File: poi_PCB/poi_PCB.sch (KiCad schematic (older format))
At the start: 43 parts

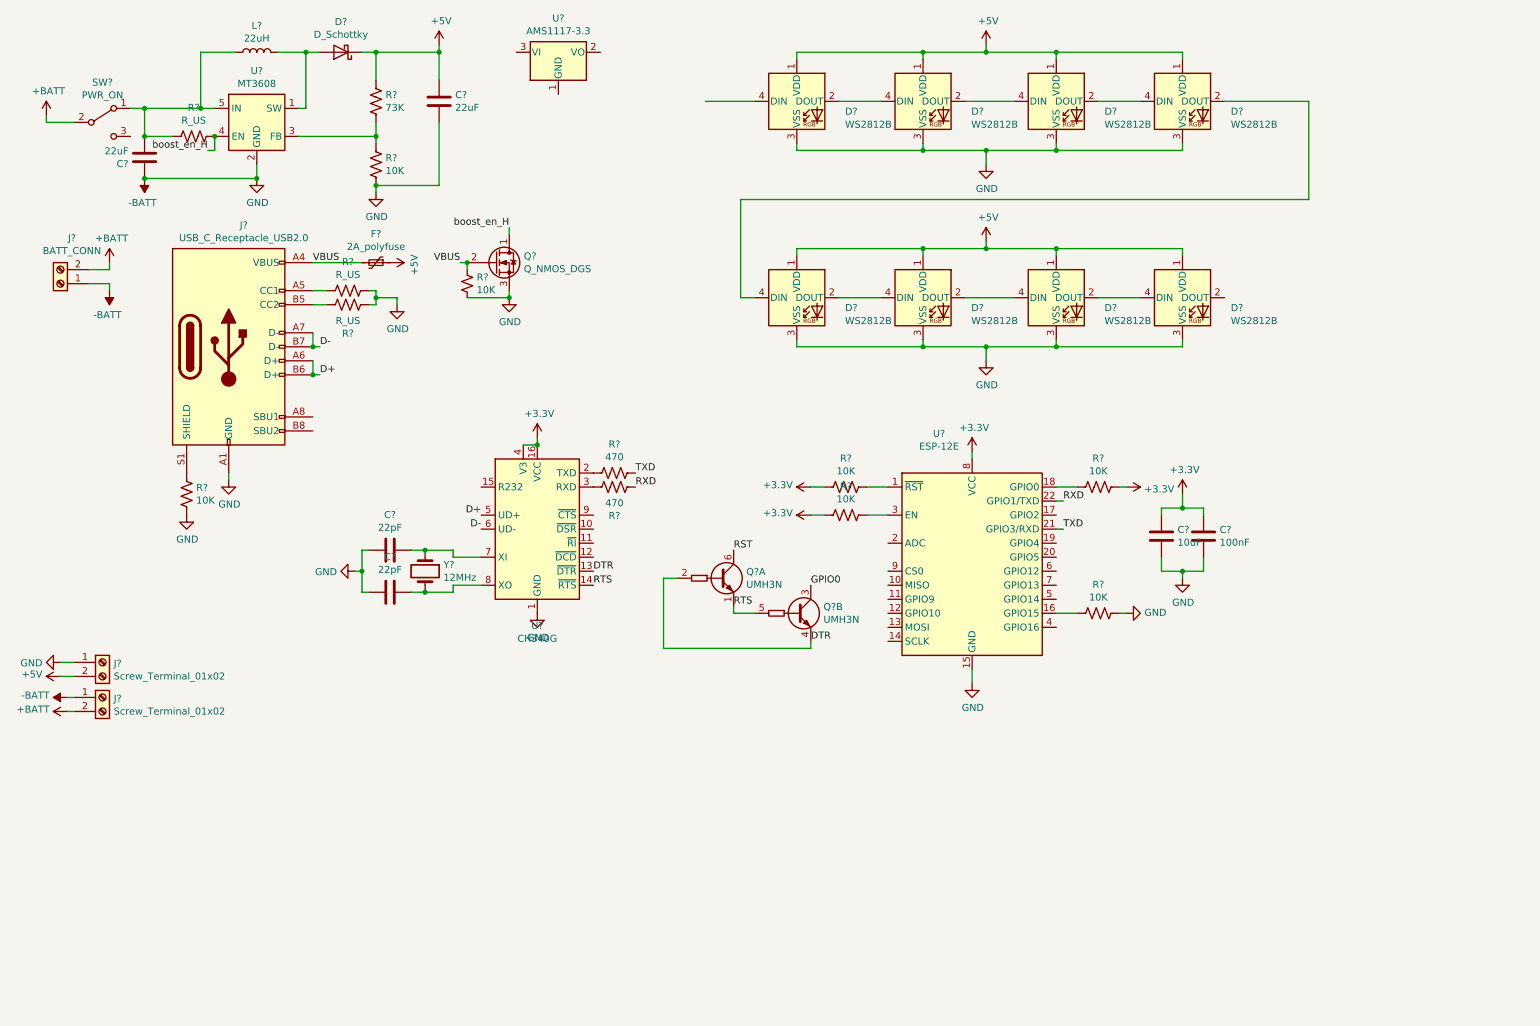
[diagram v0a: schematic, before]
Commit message: added TP4056 footprint
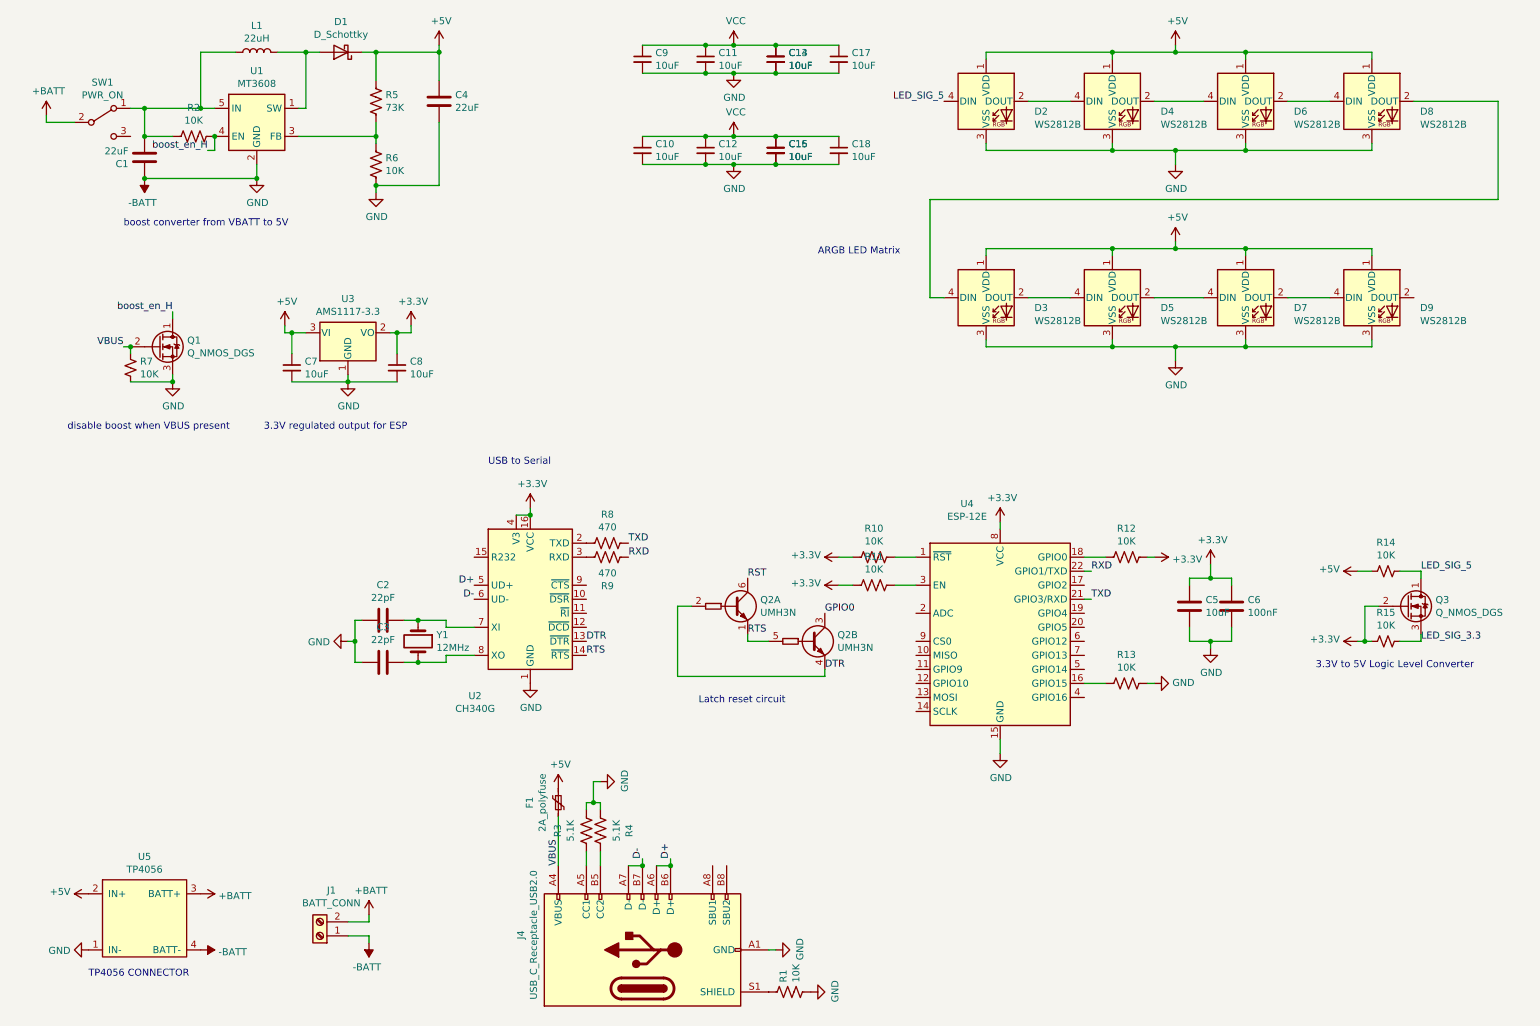
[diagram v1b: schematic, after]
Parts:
- removed J? (x2): Screw_Terminal_01x02, symbol Connector:Screw_Terminal_01x02
- added C10, C11, C12, C13, C14, C15, C16, C17, C18, C7, C8, C9: 10uF, Capacitor_SMD:C_0805_2012Metric, symbol Device:C_Small
- added Q3: Q_NMOS_DGS, Package_TO_SOT_SMD:SOT-23, symbol Device:Q_NMOS_DGS
- added R14, R15: 10K, Resistor_SMD:R_0603_1608Metric, symbol Device:R_Small_US
- added U5: TP4056, Arduino:TP4056, symbol arduino:TP4056
- C1, C4: renamed from C?; footprint (none) -> Capacitor_SMD:C_0603_1608Metric; LCSC (none) -> C59461
- C2, C3: renamed from C?; footprint (none) -> Capacitor_SMD:C_0402_1005Metric; LCSC (none) -> C1555
- C5: renamed from C?; footprint (none) -> Capacitor_SMD:C_0805_2012Metric; LCSC (none) -> C15850
- C6: renamed from C?; footprint (none) -> Capacitor_SMD:C_0402_1005Metric; LCSC (none) -> C307331
- D1: renamed from D?; footprint (none) -> Diode_SMD:D_SMA; LCSC (none) -> C22452
- D2, D3, D4, D5, D6, D7, D8, D9: renamed from D?; LCSC (none) -> C139127
- F1: renamed from F?; footprint (none) -> Fuse:Fuse_0805_2012Metric
- J1: renamed from J?; footprint (none) -> TerminalBlock_Phoenix:TerminalBlock_Phoenix_MKDS-1,5-2-5.08_1x02_P5.08mm_Horizontal
- J4: renamed from J?; footprint (none) -> Connector_USB:USB_C_Receptacle_HRO_TYPE-C-31-M-12
- L1: renamed from L?; footprint (none) -> Inductor_SMD:L_7.3x7.3_H3.5
- Q1: renamed from Q?; footprint (none) -> Package_TO_SOT_SMD:SOT-23
- R1, R10, R11, R12, R13, R5, R6, R7, R8, R9: renamed from R?; footprint (none) -> Resistor_SMD:R_0402_1005Metric
- R2: renamed from R?; value R_US -> 10K; footprint (none) -> Resistor_SMD:R_0402_1005Metric
- R3, R4: renamed from R?; value R_US -> 5.1K; footprint (none) -> Resistor_SMD:R_0402_1005Metric
- SW1: renamed from SW?; footprint (none) -> Button_Switch_SMD:SW_SPDT_PCM12
- Y1: renamed from Y?; footprint (none) -> Crystal:Crystal_SMD_0603-2Pin_6.0x3.5mm
- gave numbers to parts that had none: 5
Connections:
- net +3V3: now also U3.2 (VO), C8.1, Q3.2 (G), R15.2
- net +5V: now also U3.3 (VI), C7.1, R14.2, U5.2 (IN+)
- net +BATT: now also U5.3 (BATT+)
- net -BATT: now also U3.1 (GND), C10.2, C11.2, C12.2, C13.2, C14.2, C15.2, C16.2, C17.2, C18.2, C7.2, C8.2, C9.2, U5.1 (IN-), U5.4 (BATT-)
- net LED_SIG_5: now reaches D2.4 (DIN)
- net LED_SIG_5: now also Q3.1 (D), R14.1
- new net LED_SIG_3.3: Q3.3 (S), R15.1
- new net VCC: C10.1, C11.1, C12.1, C13.1, C14.1, C15.1, C16.1, C17.1, C18.1, C9.1
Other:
- note added: "3.3V regulated output for ESP\n"
- note added: "3.3V to 5V Logic Level Converter\n"
- note added: "ARGB LED Matrix\n"
- note added: "Latch reset circuit\n"
- note added: "TP4056 CONNECTOR\n"
- note added: "USB to Serial\n"
- note added: "boost converter from VBATT to 5V"
- note added: "disable boost when VBUS present\n"
- moved on the sheet: C2, C3, C5, C6, D2, D3, D4, D5, D6, D7, D8, D9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

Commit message: Changed USB-> Serial chip, added documentation
-CH340G replaced with CH340C to eliminate the need for a crystal
-Part sourcing updated in BOM
-minor edits based on available parts
-Schematic updated to reflect changes
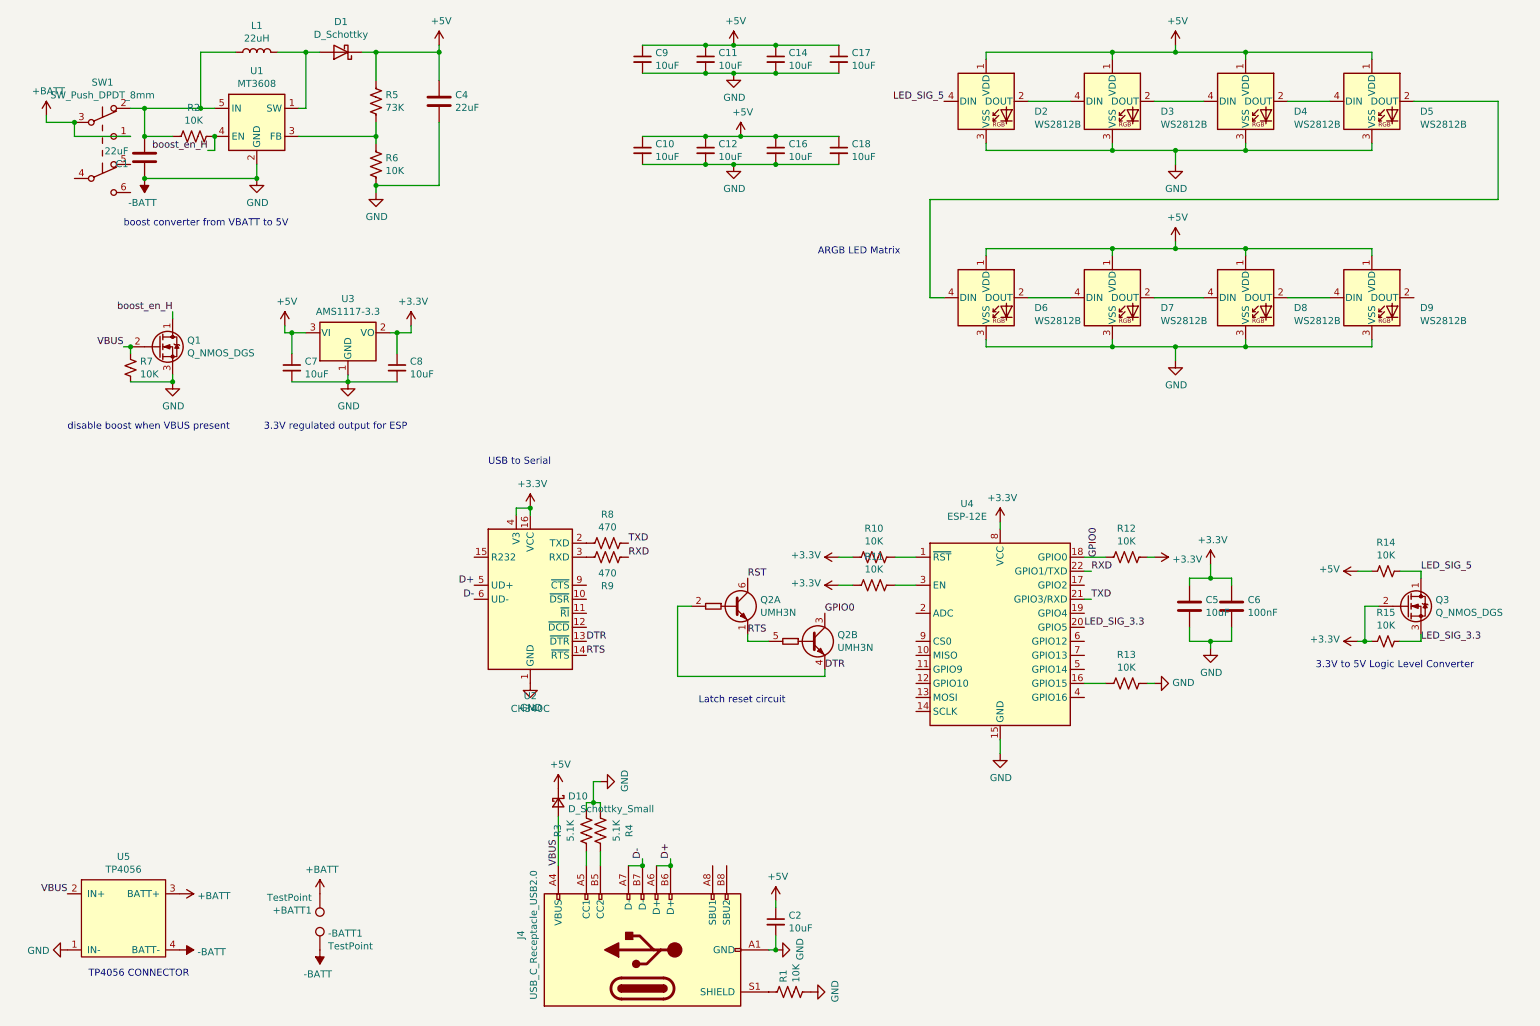
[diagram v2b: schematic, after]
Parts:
- removed C13, C15: 10uF, Capacitor_SMD:C_0805_2012Metric, symbol Device:C_Small
- removed C2, C3: 22pF, Capacitor_SMD:C_0402_1005Metric, symbol Device:C
- removed F1: 2A_polyfuse, Fuse:Fuse_0805_2012Metric, symbol Device:Polyfuse_Small
- removed J1: BATT_CONN, TerminalBlock_Phoenix:TerminalBlock_Phoenix_MKDS-1,5-2-5.08_1x02_P5.08mm_Horizontal, symbol Connector:Screw_Terminal_01x02
- removed SW1: PWR_ON, Button_Switch_SMD:SW_SPDT_PCM12, symbol Switch:SW_SPDT
- removed U2: CH340G, Package_SO:SOIC-16_3.9x9.9mm_P1.27mm, symbol Interface_USB:CH340G
- removed Y1: 12MHz, Crystal:Crystal_SMD_0603-2Pin_6.0x3.5mm, symbol Device:Crystal
- added +BATT1, -BATT1: TestPoint, TestPoint:TestPoint_THTPad_D3.0mm_Drill1.5mm, symbol Connector:TestPoint
- added C2: 10uF, Capacitor_SMD:C_0805_2012Metric, symbol Device:C_Small
- added D10: D_Schottky_Small, Diode_SMD:D_SMA, symbol Device:D_Schottky_Small
- added SW1: SW_Push_DPDT_8mm, 8mm_switch:8mm_latching_switch, symbol Switch_8mm:SW_Push_DPDT_8mm
- added U2: CH340C, Package_SO:SOIC-16_3.9x9.9mm_P1.27mm, symbol Interface_USB:CH340C
- J4: footprint Connector_USB:USB_C_Receptacle_HRO_TYPE-C-31-M-12 -> USB4120-03-C_REVA:GCT_USB4120-03-C_REVA
- L1: footprint Inductor_SMD:L_7.3x7.3_H3.5 -> Inductor_SMD:L_6.3x6.3_H3; LCSC (none) -> C207843
- Q1, Q3: LCSC (none) -> C8545
- Q2: LCSC (none) -> C62892
- R1, R10, R11, R12, R13, R2, R6, R7: LCSC (none) -> C25744
- R14, R15: LCSC (none) -> C25804
- R3, R4: LCSC (none) -> C25905
- R5: LCSC (none) -> C25798
- R8, R9: LCSC (none) -> C25117
- U3: LCSC (none) -> C6186
- renumbered D4 to D3, D6 to D4, D8 to D5, D3 to D6, D5 to D7, D7 to D8
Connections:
- net VCC is gone; now on net +5V: C10.1, C11.1, C12.1, C14.1, C16.1, C17.1, C18.1, C9.1
- net +3V3: now also U2.16 (VCC), U2.4 (V3)
- net +5V: now also C2.1, D10.1 (K); no longer U5.2 (IN+)
- net +BATT: now also +BATT1.1, SW1.1, SW1.3
- net -BATT: now also -BATT1.1, C2.2, U2.1 (GND)
- net D+: now also U2.5 (UD+)
- net D-: now also U2.6 (UD-)
- net DTR: now also U2.13 (~DTR)
- net GPIO0: now also R12.2, U4.18 (GPIO0)
- net LED_SIG_3.3: now also U4.20 (GPIO5)
- net RTS: now also U2.14 (~RTS)
- net VBUS: now also U5.2 (IN+), D10.2 (A)
- net at C1.2, L1.1, R2.2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: now also SW1.2
- net at R8.2: now also U2.2 (TXD)
- net at R9.1: now also U2.3 (RXD)
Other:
- moved on the sheet: U5

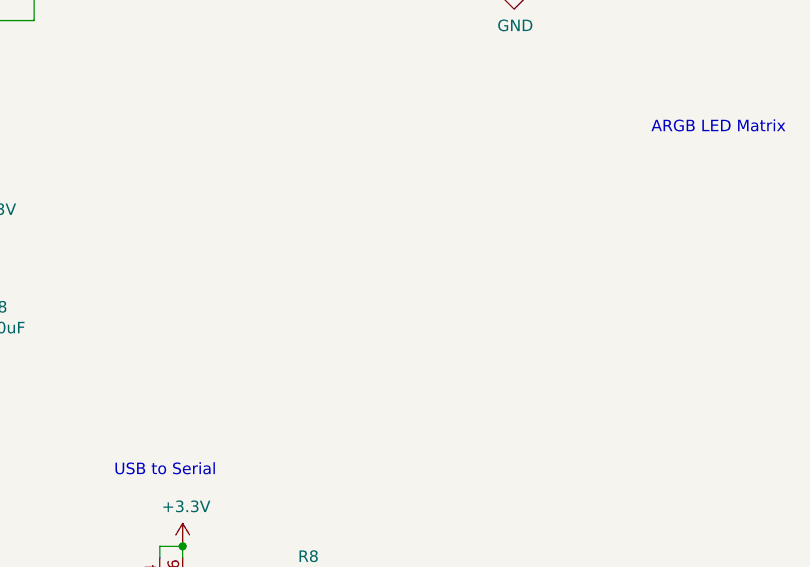
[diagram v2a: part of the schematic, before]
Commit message: Added mounting holes
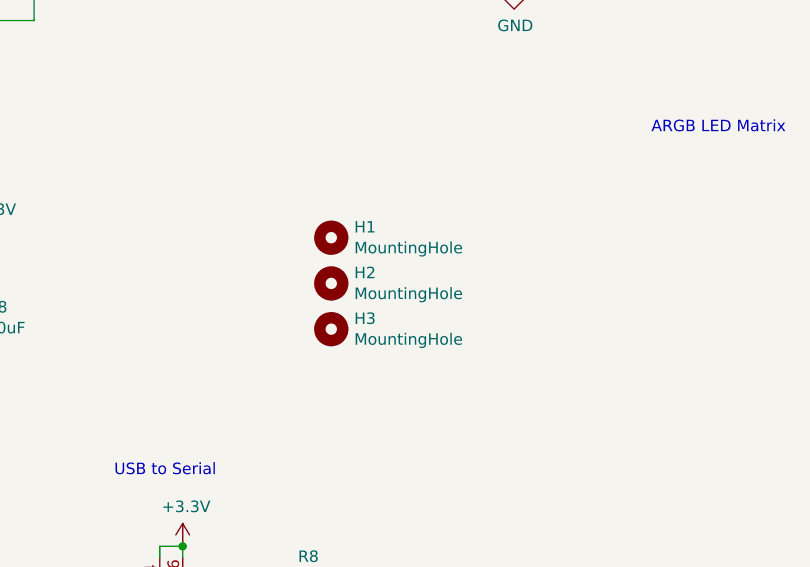
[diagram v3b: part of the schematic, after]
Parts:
- added H1, H2, H3: MountingHole, MountingHole:MountingHole_3.2mm_M3, symbol Mechanical:MountingHole
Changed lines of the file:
@@
 Wire Wire Line
 	5650 1400 5900 1400
+$Comp
+L Mechanical:MountingHole H1
+U 1 1 61A080CC
+P 4800 2700
+F 0 "H1" H 4900 2746 50  0000 L CNN
+F 1 "MountingHole" H 4900 2655 50  0000 L CNN
+F 2 "MountingHole:MountingHole_3.2mm_M3" H 4800 2700 50  0001 C CNN
+F 3 "~" H 4800 2700 50  0001 C CNN
+	1    4800 2700
+	1    0    0    -1
+$EndComp
+$Comp
+L Mechanical:MountingHole H2
+U 1 1 61A086D8
+P 4800 2900
+F 0 "H2" H 4900 2946 50  0000 L CNN
+F 1 "MountingHole" H 4900 2855 50  0000 L CNN
+F 2 "MountingHole:MountingHole_3.2mm_M3" H 4800 2900 50  0001 C CNN
+F 3 "~" H 4800 2900 50  0001 C CNN
+	1    4800 2900
+	1    0    0    -1
+$EndComp
+$Comp
+L Mechanical:MountingHole H3
+U 1 1 61A10561
+P 4800 3100
+F 0 "H3" H 4900 3146 50  0000 L CNN
+F 1 "MountingHole" H 4900 3055 50  0000 L CNN
+F 2 "MountingHole:MountingHole_3.2mm_M3" H 4800 3100 50  0001 C CNN
+F 3 "~" H 4800 3100 50  0001 C CNN
+	1    4800 3100
+	1    0    0    -1
+$EndComp
 $EndSCHEMATC
